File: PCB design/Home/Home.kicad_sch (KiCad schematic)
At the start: 18 parts, among them J1 Fan, J2 LCD, J3 EM LOCK, J4 ACS712 Signal, J5 Power In, J6 ACS712 Power, J7 RFID, J8 RFID, J9 LCD, U1 ACS712, U3 DHT11, U5 PIR, U6 MQ2

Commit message: footprints complete
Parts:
- removed U1: ACS712, Package_SO:SOIC-8_3.9x4.9mm_P1.27mm, symbol Sensor_Current_module:ACS712xLCTR-05B
- added U1: ACS712, Sensor_Current:ACS712_5B, symbol Sensor_Current_module:ACS712_5B
- BZ1: footprint Buzzer_Beeper:Buzzer_15x7.5RM7.6 -> Sensor_Current:ACS712_5B
- ESP32_DEVKIT_V1: footprint (none) -> esp32:MODULE_ESP32_DEVKIT_V1
- LM2596_buck_converter1, LM2596_buck_converter2: footprint (none) -> DC-DC_Buck_Converter:LM2596_module
- U5: footprint (none) -> Sensor_motion_PIR:PIR_HC-S501
- U6: footprint (none) -> Sensor_Gas:MQ2
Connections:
- net +3.3V: now also ESP32_DEVKIT_V1.15 (VIN); no longer ESP32_DEVKIT_V1.VIN
- net +5V: now also U1.1 (VCC)
- net 3V3: now also ESP32_DEVKIT_V1.16 (3.3V); no longer ESP32_DEVKIT_V1.3.3V
- net ACS: now also ESP32_DEVKIT_V1.4 (GPIO34), U1.2 (OUT); no longer ESP32_DEVKIT_V1.34 (GPIO34)
- net BLUE: now also ESP32_DEVKIT_V1.11 (GPIO14); no longer ESP32_DEVKIT_V1.14 (GPIO14)
- net BUZZ: now also ESP32_DEVKIT_V1.8 (GPIO25)
- net DHT: now also ESP32_DEVKIT_V1.21 (GPIO16/RXD_2); no longer ESP32_DEVKIT_V1.16 (GPIO16/RXD_2)
- net GND: now also ESP32_DEVKIT_V1.14 (GND), U1.3 (GND); no longer ESP32_DEVKIT_V1.GND1 (wGND)
- net MISO: now also ESP32_DEVKIT_V1.25 (GPIO19/MISO); no longer ESP32_DEVKIT_V1.19 (GPIO19/MISO)
- net MOSI: now also ESP32_DEVKIT_V1.30 (GPIO23/MOSI); no longer ESP32_DEVKIT_V1.23 (GPIO23/MOSI)
- net MQ2: now also ESP32_DEVKIT_V1.19 (GPIO2); no longer ESP32_DEVKIT_V1.2 (GPIO2)
- net PIR: now also ESP32_DEVKIT_V1.6 (GPIO32); no longer ESP32_DEVKIT_V1.32 (GPIO32)
- net RELAY: now also ESP32_DEVKIT_V1.24 (GPIO18/SCK); no longer ESP32_DEVKIT_V1.18 (GPIO18/SCK)
- net SCK: now also ESP32_DEVKIT_V1.29 (GPIO22/SCL); no longer ESP32_DEVKIT_V1.22 (GPIO22/SCL)
- net SDA: now also ESP32_DEVKIT_V1.7 (GPIO33); no longer ESP32_DEVKIT_V1.33 (GPIO33)
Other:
- moved on the sheet: ESP32_DEVKIT_V1

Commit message: complete schematic
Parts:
- BZ1: footprint Sensor_Current:ACS712_5B -> Buzzer_Beeper:Buzzer_D14mm_H7mm_P10mm
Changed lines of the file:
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@@
       (effects (font (size 1.27 1.27)) (justify left))
     )
-    (property "Footprint" "Sensor_Current:ACS712_5B" (at 120.015 22.86 90)
+    (property "Footprint" "Buzzer_Beeper:Buzzer_D14mm_H7mm_P10mm" (at 120.015 22.86 90)
       (effects (font (size 1.27 1.27)) hide)
     )

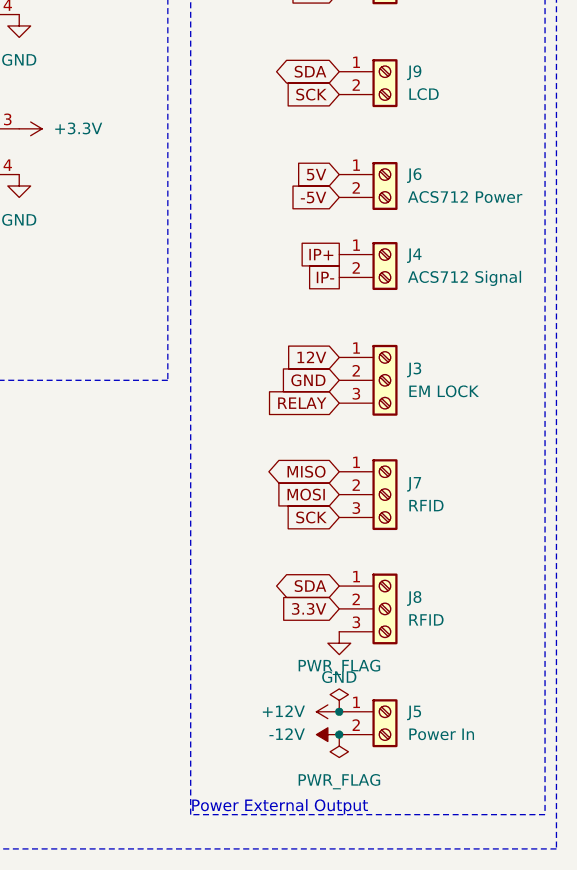
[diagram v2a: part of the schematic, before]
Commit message: PCB circuit to be completed
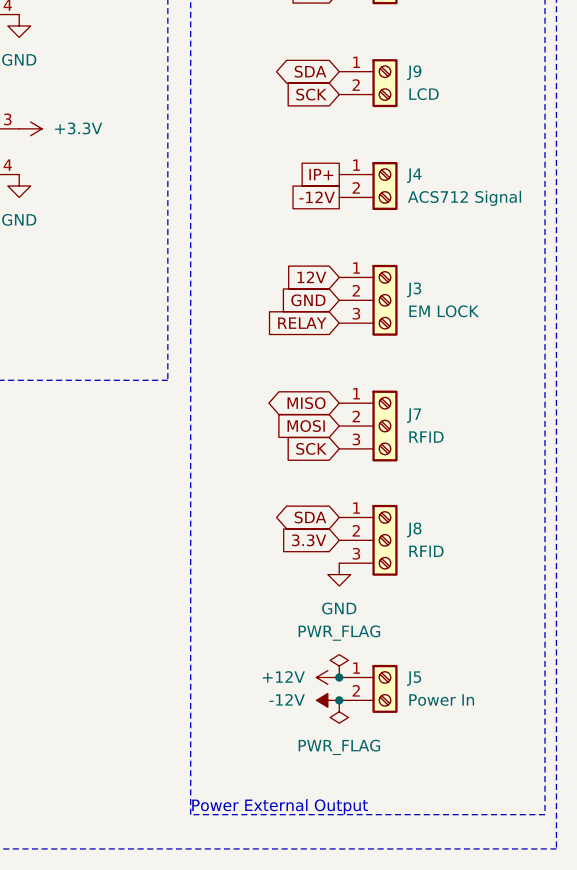
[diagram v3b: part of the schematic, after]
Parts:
- removed J6: ACS712 Power, TerminalBlock:TerminalBlock_Altech_AK300-2_P5.00mm, symbol Connector:Screw_Terminal_01x02
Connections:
- net IP- is gone; now on net -12V: J4.2 (Pin_2)
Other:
- moved on the sheet: J3, J4, J5, J7, J8

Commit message: PCB routed
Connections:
- net -5V is gone; now on net +5V: J1.2 (Pin_2), J2.2 (Pin_2)
- net 12V is gone; now on net RELAY: J3.1 (Pin_1)
- net 3.3V is gone; now on net +3.3V: J8.2 (Pin_2)
- net 5V is gone; now on net GND: J1.1 (Pin_1), J2.1 (Pin_1)
- net IP+ is gone; now on net -12V: J4.1 (Pin_1)
- net +12V: now also J3.3 (Pin_3), J5.2 (Pin_2); no longer J5.1 (Pin_1)
- net +3.3V: now also U3.1 (VDD), U5.3 (VCC)
- net -12V: now also J3.2 (Pin_2), J5.1 (Pin_1); no longer J4.2 (Pin_2), J5.2 (Pin_2)
- net 3V3: no longer U3.1 (VCC), U5.3 (VCC)
- net ACS: now also ESP32_DEVKIT_V1.24 (GPIO18/SCK); no longer ESP32_DEVKIT_V1.4 (GPIO34)
- net BLUE: now also ESP32_DEVKIT_V1.12 (GPIO12); no longer ESP32_DEVKIT_V1.11 (GPIO14)
- net BUZZ: now also ESP32_DEVKIT_V1.10 (GPIO27); no longer ESP32_DEVKIT_V1.8 (GPIO25)
- net DHT: now also ESP32_DEVKIT_V1.9 (GPIO26); no longer ESP32_DEVKIT_V1.21 (GPIO16/RXD_2)
- net GND: now also J8.1 (Pin_1); no longer J3.2 (Pin_2), J8.3 (Pin_3)
- net GREEN: now also ESP32_DEVKIT_V1.13 (GPIO13); no longer ESP32_DEVKIT_V1.12 (GPIO12)
- net MISO: now also J7.3 (Pin_3); no longer J7.1 (Pin_1)
- net MOSI: now also J8.3 (Pin_3); no longer J7.2 (Pin_2)
- net RED: now also ESP32_DEVKIT_V1.11 (GPIO14); no longer ESP32_DEVKIT_V1.13 (GPIO13)
- net RELAY: now also ESP32_DEVKIT_V1.7 (GPIO33); no longer ESP32_DEVKIT_V1.24 (GPIO18/SCK), J3.3 (Pin_3)
- net SCK: now also J7.1 (Pin_1); no longer J7.3 (Pin_3)
- net SDA: now also ESP32_DEVKIT_V1.26 (GPIO21/SDA), J7.2 (Pin_2); no longer ESP32_DEVKIT_V1.7 (GPIO33), J8.1 (Pin_1)
- no-connect marks 17 -> 18
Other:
- moved on the sheet: J5
